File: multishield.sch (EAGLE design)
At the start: 20 parts, among them J1 7p-2.54-90d, J2 2x16p-2.54, J3 7p-2.54-90d, J4 2x6p-2.54, J5 7p-2.54-90d, J6 7p-2.54-90d, K2 TS-1101F, M1 ARDUINO_R3_ICSP, SW1 SK-12D01, U1 AD595AQ-DIP14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

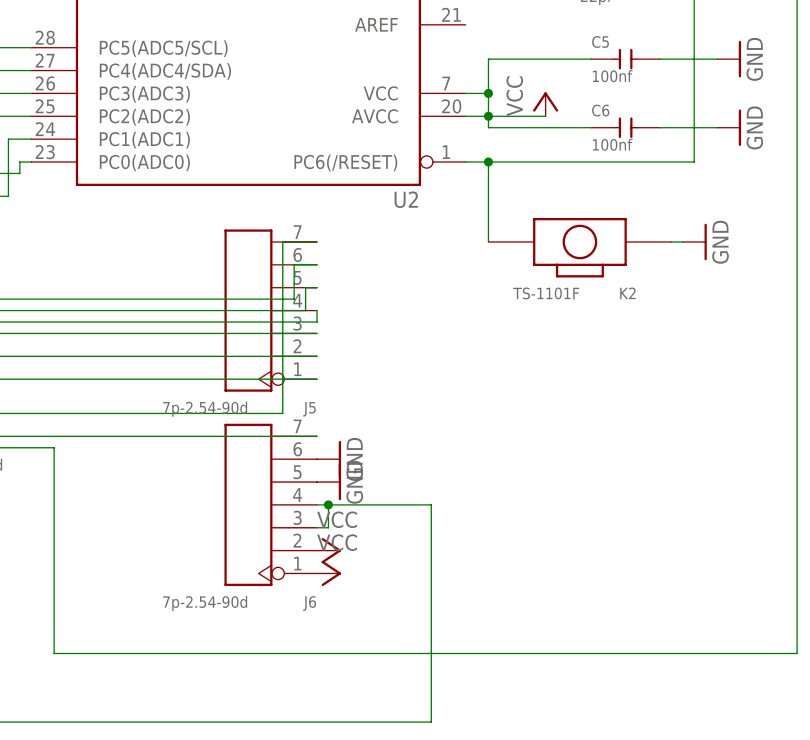
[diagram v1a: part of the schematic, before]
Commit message: reset pin added, various changes (in pin packages to make soldering easier
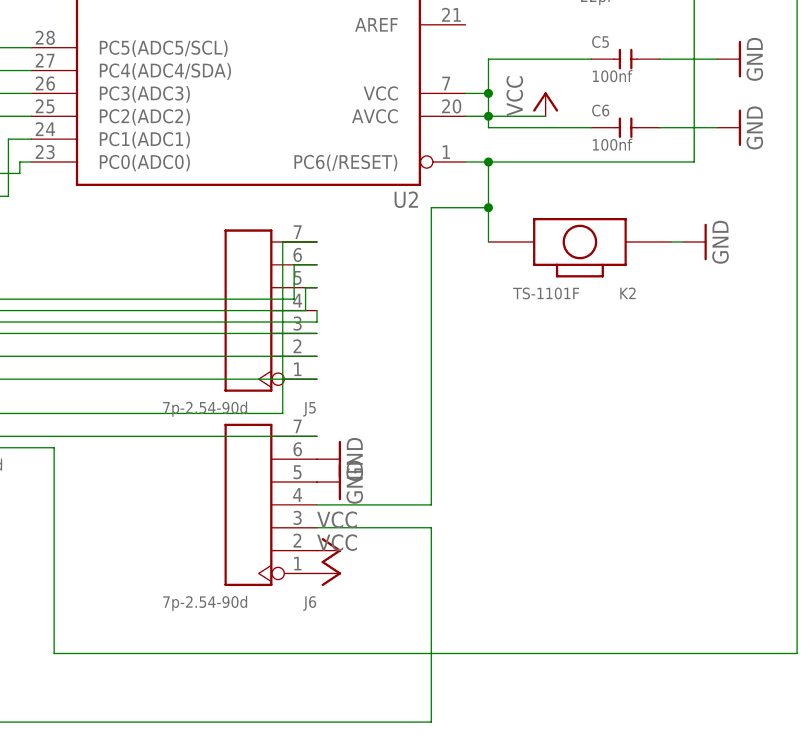
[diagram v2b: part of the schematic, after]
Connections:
- net N$54: no longer J6.4
- net SLAVE-RESET: now also J6.4
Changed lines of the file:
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@@
 <layer number="132" name="bAdjust" color="7" fill="1" visible="no" active="yes"/>
 <layer number="133" name="bottom_silk" color="7" fill="1" visible="yes" active="yes"/>
+<layer number="134" name="silk_top" color="7" fill="1" visible="no" active="no"/>
+<layer number="135" name="silk_bottom" color="7" fill="1" visible="no" active="no"/>
+<layer number="136" name="silktop" color="7" fill="1" visible="yes" active="yes"/>
+<layer number="137" name="silkbottom" color="7" fill="1" visible="yes" active="yes"/>
 <layer number="144" name="Drill_legend" color="7" fill="1" visible="no" active="yes"/>
+<layer number="145" name="DrillLegend_01-16" color="7" fill="1" visible="yes" active="yes"/>
+<layer number="146" name="DrillLegend_01-20" color="7" fill="1" visible="yes" active="yes"/>
 <layer number="150" name="Notes" color="7" fill="1" visible="no" active="yes"/>
 <layer number="151" name="HeatSink" color="7" fill="1" visible="no" active="yes"/>
@@
 <junction x="307.34" y="54.61"/>
 <pinref part="K2" gate="G$1" pin="2"/>
-<wire x1="307.34" y1="45.72" x2="307.34" y2="54.61" width="0.1524" layer="91"/>
+<wire x1="307.34" y1="45.72" x2="307.34" y2="49.53" width="0.1524" layer="91"/>
+<junction x="307.34" y="49.53"/>
+<wire x1="307.34" y1="49.53" x2="307.34" y2="54.61" width="0.1524" layer="91"/>
+<pinref part="J6" gate="G$1" pin="4"/>
+<wire x1="288.29" y1="16.51" x2="300.99" y2="16.51" width="0.1524" layer="91"/>
+<wire x1="300.99" y1="16.51" x2="300.99" y2="49.53" width="0.1524" layer="91"/>
+<wire x1="300.99" y1="49.53" x2="307.34" y2="49.53" width="0.1524" layer="91"/>
 </segment>
 </net>
@@
 <wire x1="90.17" y1="73.66" x2="90.17" y2="-7.62" width="0.1524" layer="91"/>
 <wire x1="90.17" y1="-7.62" x2="300.99" y2="-7.62" width="0.1524" layer="91"/>
-<pinref part="J6" gate="G$1" pin="4"/>
-<wire x1="300.99" y1="-7.62" x2="300.99" y2="16.51" width="0.1524" layer="91"/>
-<wire x1="300.99" y1="16.51" x2="289.56" y2="16.51" width="0.1524" layer="91"/>
-<wire x1="289.56" y1="16.51" x2="288.29" y2="16.51" width="0.1524" layer="91"/>
-<junction x="289.56" y="16.51"/>
 <pinref part="J6" gate="G$1" pin="3"/>
-<wire x1="288.29" y1="13.97" x2="289.56" y2="13.97" width="0.1524" layer="91"/>
-<wire x1="289.56" y1="13.97" x2="289.56" y2="16.51" width="0.1524" layer="91"/>
-</segment>
-</net>
+<wire x1="288.29" y1="13.97" x2="300.99" y2="13.97" width="0.1524" layer="91"/>
+<wire x1="300.99" y1="13.97" x2="300.99" y2="-7.62" width="0.1524" layer="91"/>
+</segment>
+</net>

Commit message: various improvements and addition of LED at D9
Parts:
- added D9: SR302DC, Seeed-OPL-Diode:DIP-LED-RED-RED(2P-D3MM)
- added R2: 150Ω, Seeed-OPL-Resistor:DIP-RES-1K-5%-1/4W(PR-D2.3XL6.5MM)
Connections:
- net N$18 renamed D9A
- removed net N$34: J2.23, J5.1, U2.PB1(OC1A)
- new net D9B: D9.+, J2.23, J5.1, U2.PB1(OC1A)
- new net N$18: D9.-, R2.1
- net GND: now also R2.2
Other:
- note added: "D9"
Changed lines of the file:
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@@
 <setting verticaltext="up"/>
 </settings>
-<grid distance="0.1" unitdist="inch" unit="inch" style="lines" multiple="1" display="no" altdistance="0.01" altunitdist="inch" altunit="inch"/>
+<grid distance="0.05" unitdist="inch" unit="inch" style="lines" multiple="1" display="no" altdistance="0.01" altunitdist="inch" altunit="inch"/>
 <layers>
 <layer number="1" name="Top" color="4" fill="1" visible="no" active="no"/>
@@
 <part name="P+8" library="supply1" deviceset="VCC" device=""/>
 <part name="GND14" library="supply1" deviceset="GND" device=""/>
+<part name="D9" library="Seeed-OPL-Diode" deviceset="DIP-LED-RED-RED(2P-D3MM)" device="" value="SR302DC"/>
+<part name="R2" library="Seeed-OPL-Resistor" deviceset="DIP-RES-1K-5%-1/4W(PR-D2.3XL6.5MM)" device="" value="150Ω"/>
+<part name="GND10" library="supply1" deviceset="GND" device=""/>
 </parts>
 <sheets>
@@
 <text x="213.36" y="198.12" size="5.08" layer="97" align="bottom-center">Arduino Multishield
 rev. 0</text>
+<text x="95.25" y="135.89" size="1.778" layer="95">D9</text>
 </plain>
 <instances>
@@
 <instance part="P+8" gate="VCC" x="290.83" y="8.89" rot="R270"/>
 <instance part="GND14" gate="1" x="290.83" y="19.05" rot="R90"/>
+<instance part="D9" gate="G$1" x="93.98" y="148.59" rot="R90"/>
+<instance part="R2" gate="G$1" x="93.98" y="156.21" rot="R90"/>
+<instance part="GND10" gate="1" x="93.98" y="162.306" rot="R180"/>
 </instances>
 <busses>
@@
 </segment>
 </net>
-<net name="N$18" class="0">
+<net name="D9A" class="0">
 <segment>
 <pinref part="J2" gate="G$1" pin="10"/>
@@
 </segment>
 </net>
-<net name="N$34" class="0">
+<net name="D9B" class="0">
 <segment>
 <pinref part="J2" gate="G$1" pin="23"/>
@@
 <wire x1="189.23" y1="30.48" x2="288.29" y2="30.48" width="0.1524" layer="91"/>
 <pinref part="J5" gate="G$1" pin="1"/>
+</segment>
+<segment>
+<pinref part="D9" gate="G$1" pin="+"/>
+<wire x1="93.98" y1="144.78" x2="93.98" y2="135.89" width="0.1524" layer="91"/>
 </segment>
 </net>
@@
 <pinref part="K2" gate="G$1" pin="1"/>
 <wire x1="327.66" y1="45.72" x2="328.93" y2="45.72" width="0.1524" layer="91"/>
+</segment>
+<segment>
+<pinref part="R2" gate="G$1" pin="2"/>
+<pinref part="GND10" gate="1" pin="GND"/>
+<wire x1="93.98" y1="159.766" x2="93.98" y2="160.02" width="0.1524" layer="91"/>
 </segment>
 </net>
@@
 </segment>
 </net>
+<net name="N$18" class="0">
+<segment>
+<pinref part="D9" gate="G$1" pin="-"/>
+<pinref part="R2" gate="G$1" pin="1"/>
+</segment>
+</net>

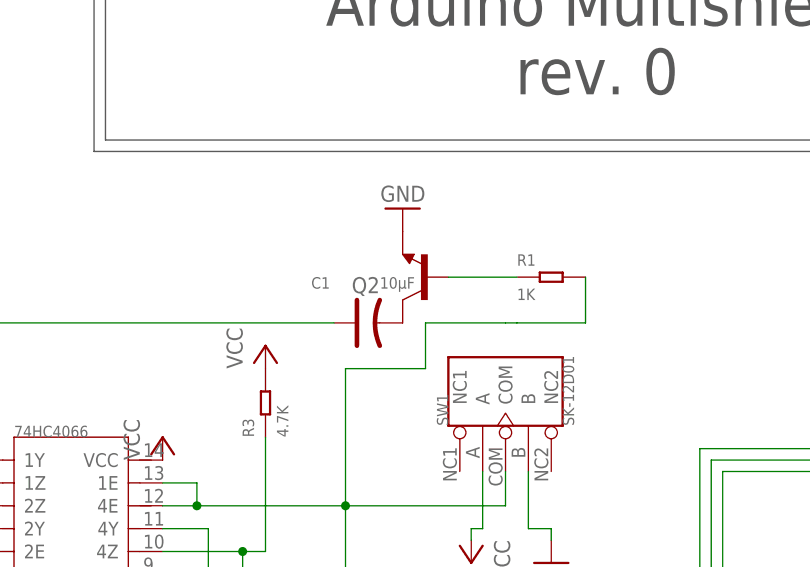
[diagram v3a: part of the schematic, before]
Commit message: changed 0 and 1 labels to rx and tx
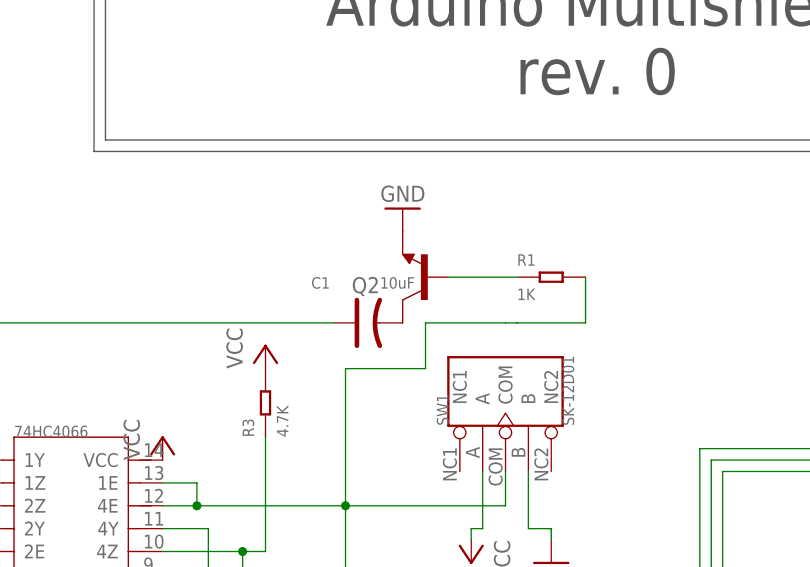
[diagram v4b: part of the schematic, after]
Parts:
- C1: value 10µF -> 10uF
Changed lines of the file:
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@@
 <part name="GND11" library="supply1" deviceset="GND" device=""/>
 <part name="K2" library="Seeed-OPL-Button" deviceset="DIP-BUTTON-FRONT-WHITE(2P-3.4X6MM)" device="" value="TS-1101F"/>
-<part name="C1" library="Seeed-OPL-Capacitor" deviceset="DIP-CAP-ALUMINUM-47UF-16V(D5-H9MM)" device="" value="10µF"/>
+<part name="C1" library="Seeed-OPL-Capacitor" deviceset="DIP-CAP-ALUMINUM-47UF-16V(D5-H9MM)" device="" value="10uF"/>
 <part name="GND5" library="supply1" deviceset="GND" device=""/>
 <part name="R1" library="Seeed-OPL-Resistor" deviceset="DIP-RES-1K-5%-1/4W(PR-D2.3XL6.5MM)" device="" value="1K"/>

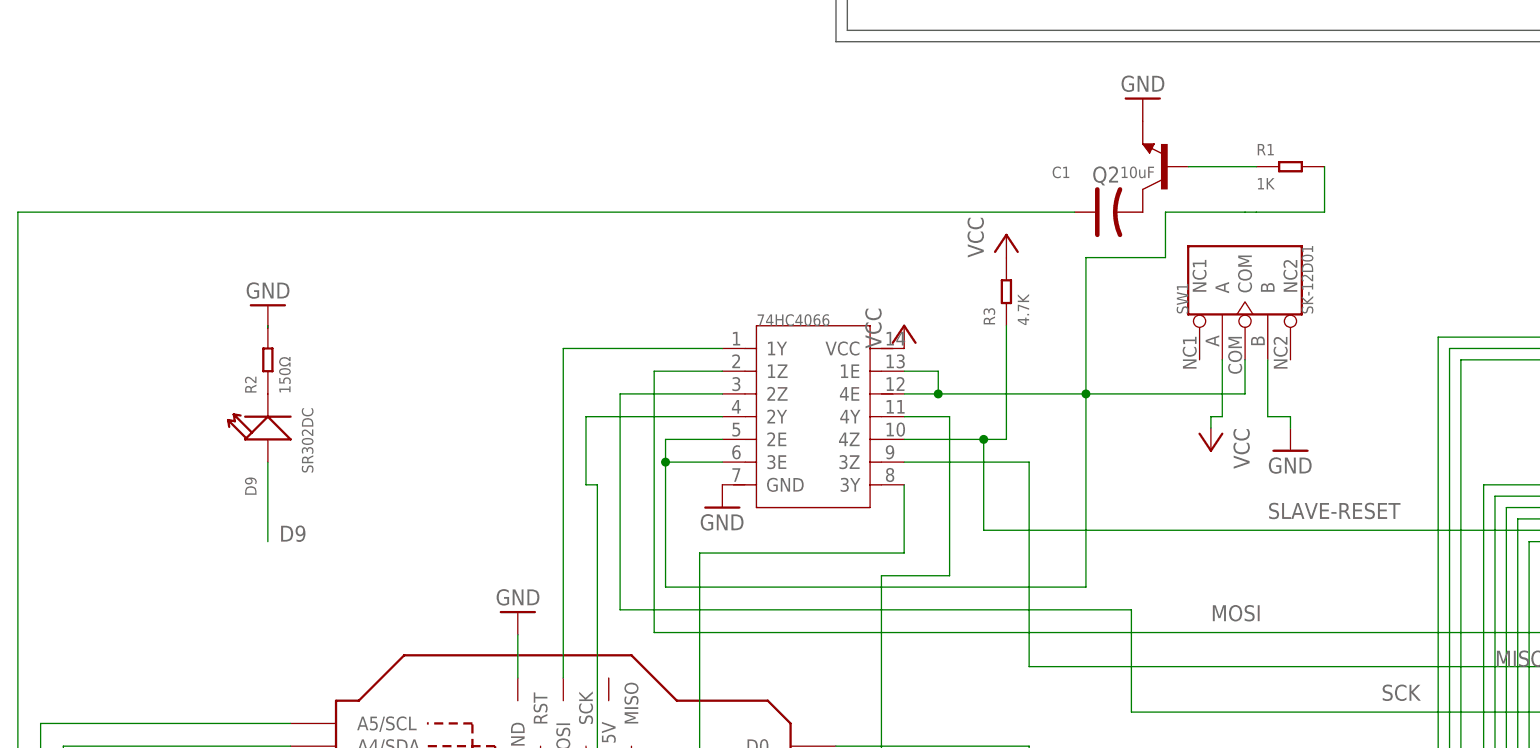
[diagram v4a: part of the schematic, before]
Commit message: no more short circuiting while switch in the middle position
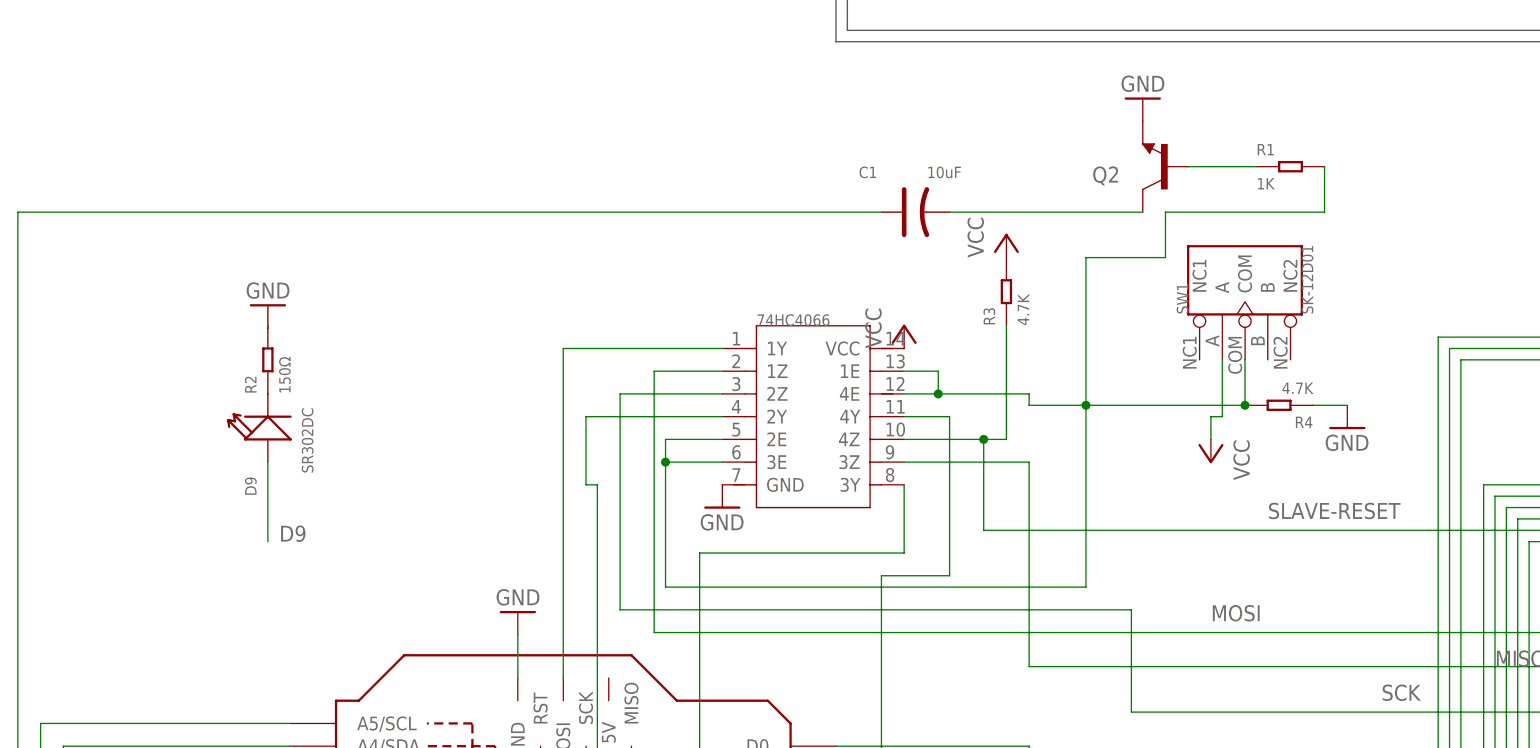
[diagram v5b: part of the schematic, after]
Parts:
- added R4: 4.7K, Seeed-OPL-Resistor:DIP-RES-4.7K-5%-1/4W(PR-D2.3XL6.5MM)
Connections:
- net GND: now also R4.1; no longer SW1.B
- net N$56: now also R4.2
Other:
- moved on the sheet: C1
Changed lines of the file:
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@@
 <part name="R2" library="Seeed-OPL-Resistor" deviceset="DIP-RES-1K-5%-1/4W(PR-D2.3XL6.5MM)" device="" value="150Ω"/>
 <part name="GND10" library="supply1" deviceset="GND" device=""/>
+<part name="R4" library="Seeed-OPL-Resistor" deviceset="DIP-RES-4.7K-5%-1/4W(PR-D2.3XL6.5MM)" device="" value="4.7K"/>
 </parts>
 <sheets>
@@
 <instance part="P+3" gate="VCC" x="165.1" y="160.02"/>
 <instance part="SW1" gate="G$1" x="203.2" y="165.1" rot="R90"/>
-<instance part="P+4" gate="VCC" x="199.39" y="146.05" rot="R180"/>
+<instance part="P+4" gate="VCC" x="199.39" y="144.78" rot="R180"/>
 <instance part="R3" gate="G$1" x="176.53" y="163.83" rot="R90"/>
 <instance part="P+5" gate="VCC" x="176.53" y="170.18"/>
-<instance part="GND8" gate="1" x="208.28" y="146.05"/>
+<instance part="GND8" gate="1" x="214.63" y="148.59"/>
 <instance part="GND11" gate="1" x="331.47" y="45.72" rot="R90"/>
 <instance part="K2" gate="G$1" x="317.5" y="45.72" rot="R180"/>
-<instance part="C1" gate="G$1" x="187.96" y="172.72"/>
+<instance part="C1" gate="G$1" x="166.37" y="172.72"/>
 <instance part="GND5" gate="1" x="191.77" y="185.42" rot="R180"/>
 <instance part="R1" gate="G$1" x="208.28" y="177.8"/>
@@
 <instance part="R2" gate="G$1" x="93.98" y="156.21" rot="R90"/>
 <instance part="GND10" gate="1" x="93.98" y="162.306" rot="R180"/>
+<instance part="R4" gate="G$1" x="207.01" y="151.13" rot="R180"/>
 </instances>
 <busses>
@@
 <pinref part="P+4" gate="VCC" pin="VCC"/>
 <wire x1="200.66" y1="149.86" x2="199.39" y2="149.86" width="0.1524" layer="91"/>
-<wire x1="199.39" y1="149.86" x2="199.39" y2="148.59" width="0.1524" layer="91"/>
+<wire x1="199.39" y1="149.86" x2="199.39" y2="147.32" width="0.1524" layer="91"/>
 </segment>
 <segment>
@@
 </segment>
 <segment>
-<pinref part="SW1" gate="G$1" pin="B"/>
-<wire x1="205.74" y1="156.21" x2="205.74" y2="149.86" width="0.1524" layer="91"/>
-<pinref part="GND8" gate="1" pin="GND"/>
-<wire x1="205.74" y1="149.86" x2="208.28" y2="149.86" width="0.1524" layer="91"/>
-<wire x1="208.28" y1="149.86" x2="208.28" y2="148.59" width="0.1524" layer="91"/>
-</segment>
-<segment>
 <pinref part="C3" gate="G$1" pin="2"/>
 <pinref part="C2" gate="G$1" pin="1"/>
@@
 <pinref part="GND10" gate="1" pin="GND"/>
 <wire x1="93.98" y1="159.766" x2="93.98" y2="160.02" width="0.1524" layer="91"/>
+</segment>
+<segment>
+<pinref part="R4" gate="G$1" pin="1"/>
+<pinref part="GND8" gate="1" pin="GND"/>
+<wire x1="210.82" y1="151.13" x2="214.63" y2="151.13" width="0.1524" layer="91"/>
 </segment>
 </net>
@@
 </segment>
 </net>
-<net name="N$56" class="0">
-<segment>
-<pinref part="U1" gate="74HC4066" pin="3E"/>
-<wire x1="144.78" y1="144.78" x2="138.43" y2="144.78" width="0.1524" layer="91"/>
-<wire x1="138.43" y1="144.78" x2="138.43" y2="130.81" width="0.1524" layer="91"/>
-<wire x1="138.43" y1="130.81" x2="185.42" y2="130.81" width="0.1524" layer="91"/>
-<wire x1="185.42" y1="130.81" x2="185.42" y2="152.4" width="0.1524" layer="91"/>
-<pinref part="U1" gate="74HC4066" pin="4E"/>
-<wire x1="203.2" y1="152.4" x2="185.42" y2="152.4" width="0.1524" layer="91"/>
-<junction x="168.91" y="152.4"/>
-<wire x1="185.42" y1="152.4" x2="168.91" y2="152.4" width="0.1524" layer="91"/>
-<wire x1="168.91" y1="152.4" x2="165.1" y2="152.4" width="0.1524" layer="91"/>
-<pinref part="U1" gate="74HC4066" pin="1E"/>
-<wire x1="165.1" y1="154.94" x2="168.91" y2="154.94" width="0.1524" layer="91"/>
-<wire x1="168.91" y1="154.94" x2="168.91" y2="152.4" width="0.1524" layer="91"/>
-<junction x="185.42" y="152.4"/>
-<junction x="138.43" y="144.78"/>
-<pinref part="U1" gate="74HC4066" pin="2E"/>
-<wire x1="144.78" y1="147.32" x2="138.43" y2="147.32" width="0.1524" layer="91"/>
-<wire x1="138.43" y1="147.32" x2="138.43" y2="144.78" width="0.1524" layer="91"/>
-<pinref part="SW1" gate="G$1" pin="COM"/>
-<wire x1="203.2" y1="152.4" x2="203.2" y2="156.21" width="0.1524" layer="91"/>
-<wire x1="185.42" y1="152.4" x2="185.42" y2="167.64" width="0.1524" layer="91"/>
-<wire x1="185.42" y1="167.64" x2="194.31" y2="167.64" width="0.1524" layer="91"/>
-<wire x1="194.31" y1="167.64" x2="194.31" y2="172.72" width="0.1524" layer="91"/>
-<wire x1="194.31" y1="172.72" x2="203.2" y2="172.72" width="0.1524" layer="91"/>
-<pinref part="R1" gate="G$1" pin="2"/>
-<wire x1="203.2" y1="172.72" x2="204.47" y2="172.72" width="0.1524" layer="91"/>
-<wire x1="204.47" y1="172.72" x2="212.09" y2="172.72" width="0.1524" layer="91"/>
-<wire x1="212.09" y1="172.72" x2="212.09" y2="177.8" width="0.1524" layer="91"/>
-</segment>
-</net>
 <net name="SCK" class="0">
 <segment>
@@
 <wire x1="66.04" y1="85.09" x2="66.04" y2="172.72" width="0.1524" layer="91"/>
 <pinref part="C1" gate="G$1" pin="+"/>
-<wire x1="66.04" y1="172.72" x2="184.15" y2="172.72" width="0.1524" layer="91"/>
+<wire x1="66.04" y1="172.72" x2="162.56" y2="172.72" width="0.1524" layer="91"/>
 </segment>
 </net>
@@
 <pinref part="C1" gate="G$1" pin="-"/>
 <pinref part="Q2" gate="G$1" pin="C"/>
+<wire x1="170.18" y1="172.72" x2="191.77" y2="172.72" width="0.1524" layer="91"/>
 </segment>
 </net>
@@
 </segment>
 </net>
+<net name="N$56" class="0">
+<segment>
+<pinref part="U1" gate="74HC4066" pin="4E"/>
+<pinref part="U1" gate="74HC4066" pin="1E"/>
+<wire x1="165.1" y1="154.94" x2="168.91" y2="154.94" width="0.1524" layer="91"/>
+<wire x1="168.91" y1="154.94" x2="168.91" y2="152.4" width="0.1524" layer="91"/>
+<wire x1="168.91" y1="152.4" x2="165.1" y2="152.4" width="0.1524" layer="91"/>
+<junction x="168.91" y="152.4"/>
+<wire x1="168.91" y1="152.4" x2="179.07" y2="152.4" width="0.1524" layer="91"/>
+<wire x1="179.07" y1="152.4" x2="179.07" y2="151.13" width="0.1524" layer="91"/>
+<pinref part="U1" gate="74HC4066" pin="3E"/>
+<wire x1="144.78" y1="144.78" x2="138.43" y2="144.78" width="0.1524" layer="91"/>
+<wire x1="138.43" y1="144.78" x2="138.43" y2="130.81" width="0.1524" layer="91"/>
+<wire x1="138.43" y1="130.81" x2="185.42" y2="130.81" width="0.1524" layer="91"/>
+<wire x1="185.42" y1="130.81" x2="185.42" y2="151.13" width="0.1524" layer="91"/>
+<wire x1="203.2" y1="151.13" x2="185.42" y2="151.13" width="0.1524" layer="91"/>
+<junction x="185.42" y="151.13"/>
+<junction x="138.43" y="144.78"/>
+<pinref part="U1" gate="74HC4066" pin="2E"/>
+<wire x1="144.78" y1="147.32" x2="138.43" y2="147.32" width="0.1524" layer="91"/>
+<wire x1="138.43" y1="147.32" x2="138.43" y2="144.78" width="0.1524" layer="91"/>
+<pinref part="SW1" gate="G$1" pin="COM"/>
+<wire x1="203.2" y1="151.13" x2="203.2" y2="156.21" width="0.1524" layer="91"/>
+<wire x1="185.42" y1="151.13" x2="185.42" y2="167.64" width="0.1524" layer="91"/>
+<wire x1="185.42" y1="167.64" x2="194.31" y2="167.64" width="0.1524" layer="91"/>
+<wire x1="194.31" y1="167.64" x2="194.31" y2="172.72" width="0.1524" layer="91"/>
+<pinref part="R1" gate="G$1" pin="2"/>
+<wire x1="194.31" y1="172.72" x2="212.09" y2="172.72" width="0.1524" layer="91"/>
+<wire x1="212.09" y1="172.72" x2="212.09" y2="177.8" width="0.1524" layer="91"/>
+<pinref part="R4" gate="G$1" pin="2"/>
+<junction x="203.2" y="151.13"/>
+<wire x1="179.07" y1="151.13" x2="185.42" y2="151.13" width="0.1524" layer="91"/>
+</segment>
+</net>
